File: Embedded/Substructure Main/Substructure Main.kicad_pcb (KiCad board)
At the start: 2 copper layers, 38 parts, among them U1 G0 FFC, U2 G1 FFC, U3 S FFC, U4 USB2513B_Bi, U5 MCP7940N-xMNY, U6 INA220AIDGSR

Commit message: Modified PCB Layout to allow component clusters
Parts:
- added C23: 22uF, Capacitor_SMD:C_0603_1608Metric_Pad1.08x0.95mm_HandSolder, F.Cu at (29.0, 169.9)
- added C24: 0.1uF, Capacitor_SMD:C_0603_1608Metric_Pad1.08x0.95mm_HandSolder, F.Cu at (29.0, 168.4)
- added C25: 1uF, Capacitor_SMD:C_0603_1608Metric_Pad1.08x0.95mm_HandSolder, F.Cu at (171.8, 173.0)
- added D1: WS2812B-2020, LED_SMD:LED_WS2812B-2020_PLCC4_2.0x2.0mm, F.Cu at (171.8, 175.0)
- added J1: MicroSD, Micro SD:MicroSD_473092651, F.Cu at (27.3, 172.4)
- added U8: F FFC, FFC:FFC-8-0.5, F.Cu at (114.0, 57.4)
- C1: footprint Capacitor_SMD:C_0603_1608Metric -> Capacitor_SMD:C_0603_1608Metric_Pad1.08x0.95mm_HandSolder
- moved C19 177.3 mm to (102.2, 171.6), turned to 180 degrees
- moved C17 173.9 mm to (96.1, 172.4), turned to 180 degrees
- moved U5 173.8 mm to (101.6, 173.6)
- moved C18 170.8 mm to (96.1, 173.9), turned to 180 degrees
- moved C21 160.8 mm to (63.2, 173.0), turned to 90 degrees
- moved R9 155.5 mm to (65.8, 173.8), turned to 180 degrees
- moved U6 152.8 mm to (57.2, 173.2)
- moved C20 152.4 mm to (58.8, 175.8), turned to 180 degrees
- moved R10 151.6 mm to (65.8, 172.2), turned to 180 degrees
- moved C16 37.0 mm to (140.0, 164.8), turned to -90 degrees
- moved C15 34.2 mm to (138.5, 164.8), turned to -90 degrees
- moved R7 31.5 mm to (139.3, 167.1), turned to 180 degrees
- moved C4 27.3 mm to (137.8, 179.2), turned to -90 degrees
- moved C7 25.4 mm to (136.5, 168.5), turned to 90 degrees
- moved C5 25.0 mm to (136.2, 179.2), turned to -90 degrees
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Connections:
- net USB2M renamed HUD USB -
- net USB2P renamed HUD USB +
- ESP1 pad 13: USB1P -> Main USB -
- ESP1 pad 14: USB1M -> Main USB +
- U1 pad 7: unconnected-(U1-Pad7) -> Photoresistor 1
- U2 pad 7: unconnected-(U2-Pad7) -> Photoresistor 2
- U4 pad 1: USB1M -> Main USB -
- U4 pad 2: USB1P -> Main USB +
- U4 pad 6: USB3M -> Snoot USB -
- U4 pad 7: USB3P -> Snoot USB +

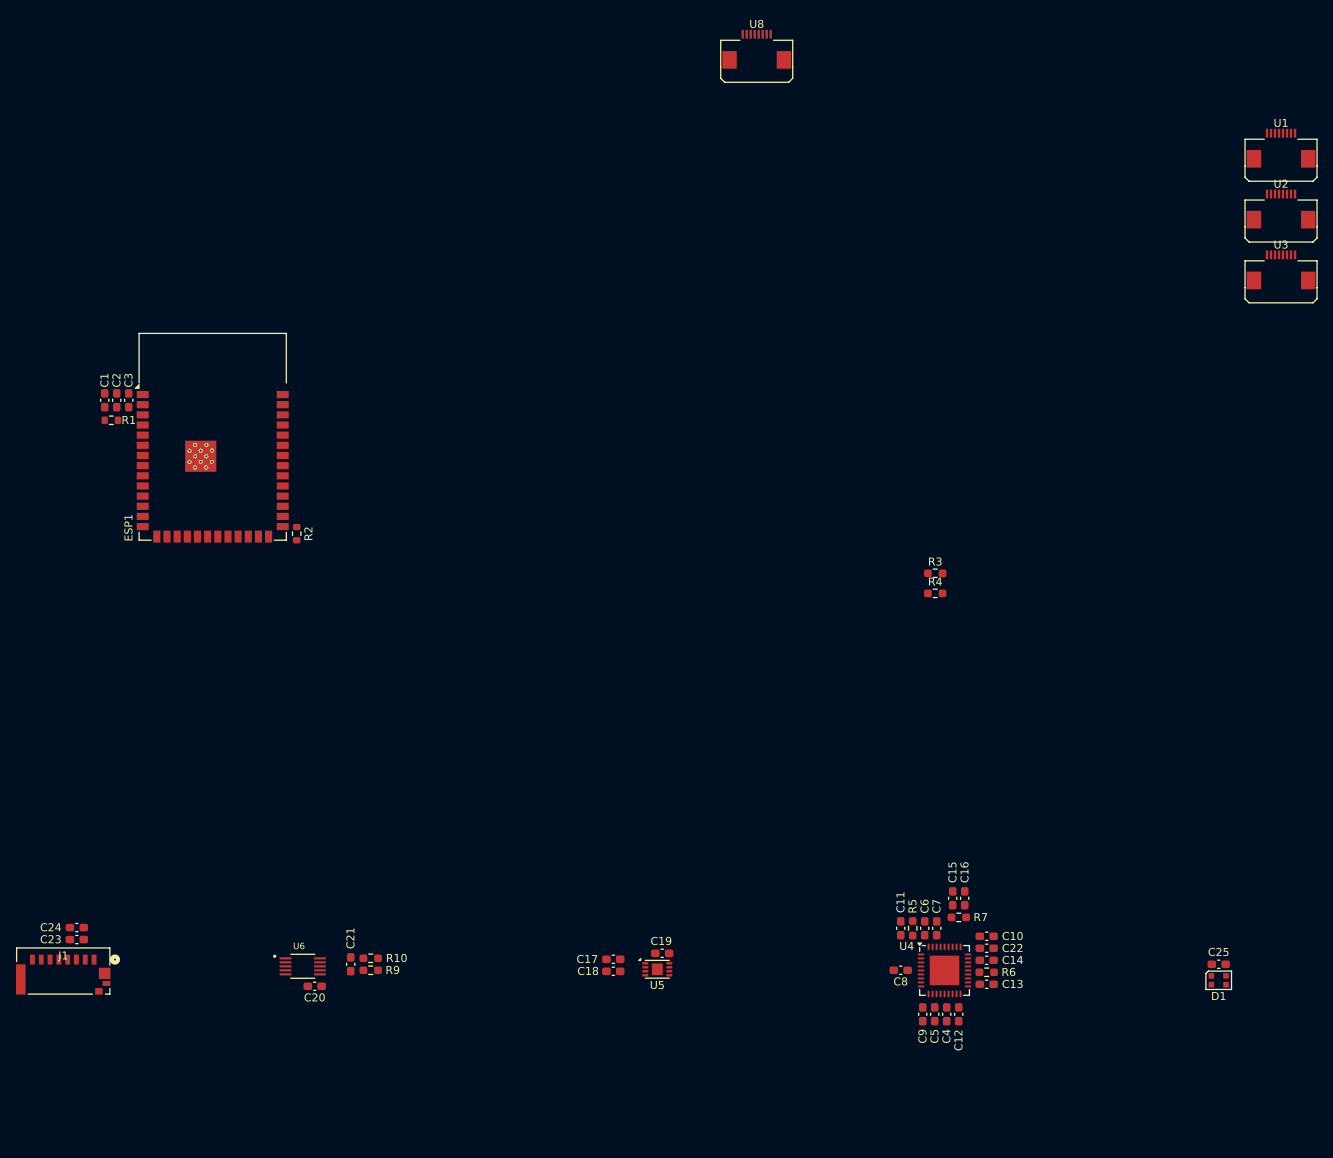
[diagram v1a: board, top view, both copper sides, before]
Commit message: Added Crystal Selection for RTC
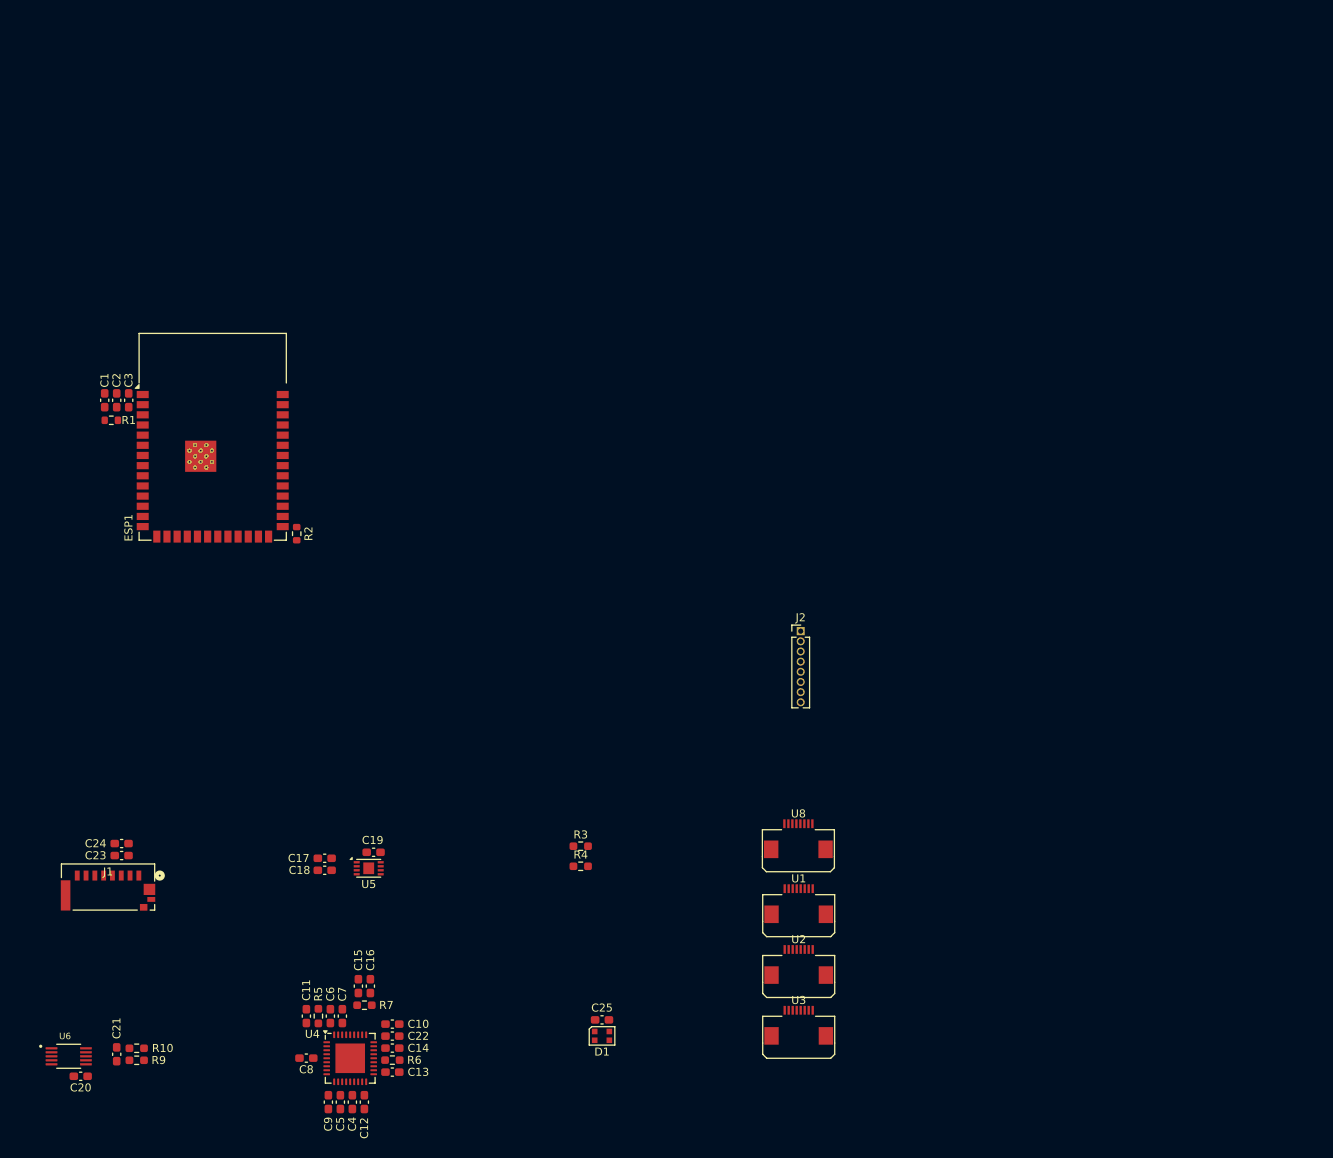
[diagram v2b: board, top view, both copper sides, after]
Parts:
- added J2: C Pins, Connector_PinHeader_1.27mm:PinHeader_1x08_P1.27mm_Vertical, F.Cu at (119.5, 131.4)
- moved U2 112.0 mm to (119.2, 171.8)
- moved U3 112.0 mm to (119.2, 179.4)
- moved U1 112.0 mm to (119.2, 164.2)
- moved U8 98.8 mm to (119.2, 156.1)
- moved C25 77.4 mm to (94.7, 179.9)
- moved D1 77.4 mm to (94.7, 181.9)
- moved C10 75.1 mm to (68.5, 180.5)
- moved C12 75.1 mm to (65.0, 190.2)
- moved C13 75.1 mm to (68.5, 186.5)
- moved C14 75.1 mm to (68.5, 183.5)
- moved C15 75.1 mm to (64.2, 175.7)
- moved C16 75.1 mm to (65.7, 175.7)
- moved C22 75.1 mm to (68.5, 182.0)
- moved R6 75.1 mm to (68.5, 185.0)
- moved R7 75.1 mm to (65.0, 178.1)
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
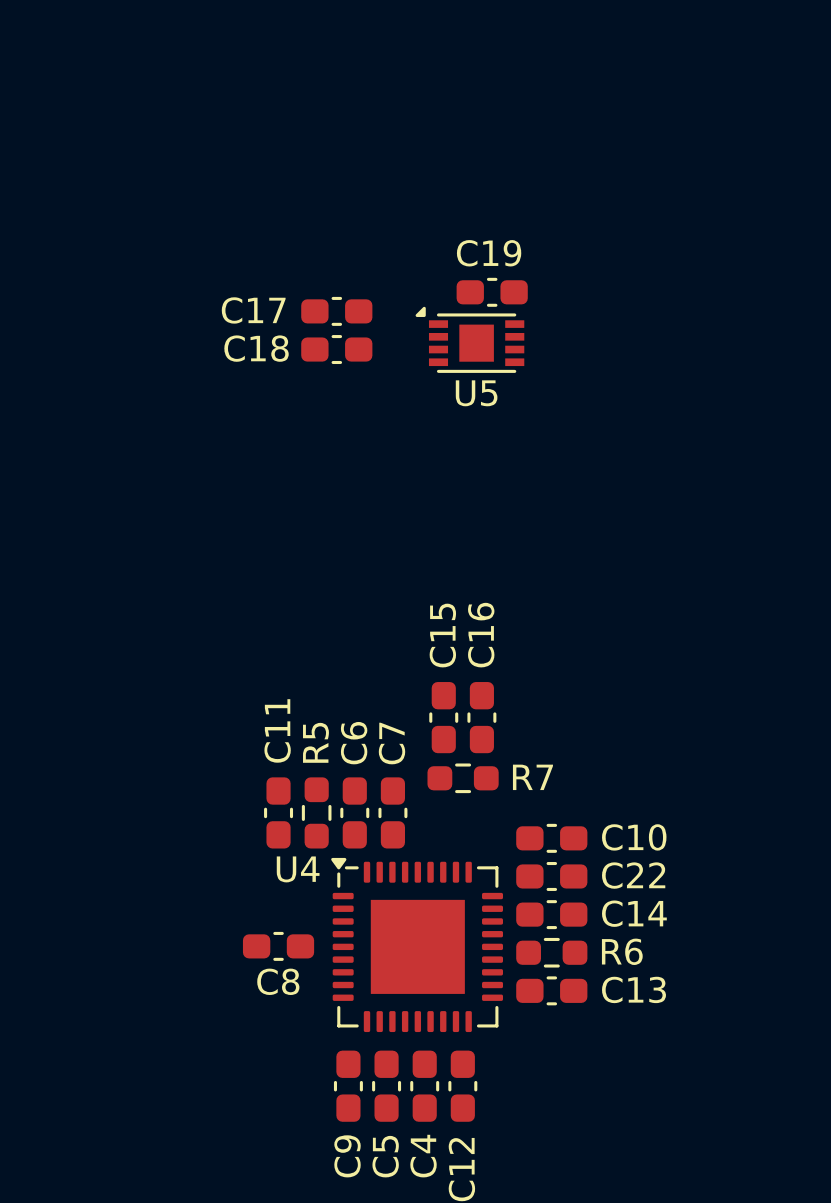
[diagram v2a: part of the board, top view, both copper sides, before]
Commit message: Added USB HUB Crystal
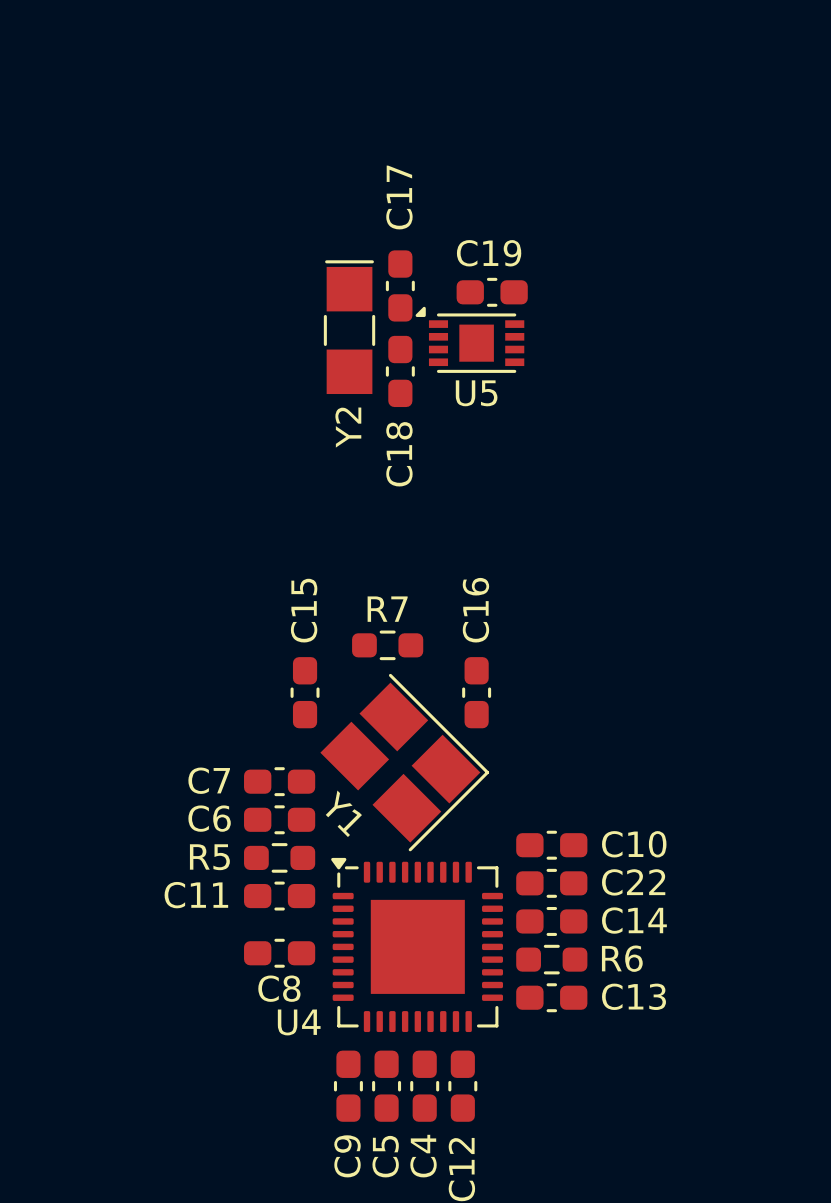
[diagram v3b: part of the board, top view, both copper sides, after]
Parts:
- added Y1: 24MHz 18pF, Crystal:Crystal_SMD_SeikoEpson_TSX3225-4Pin_3.2x2.5mm_HandSoldering, F.Cu at (62.5, 177.5)
- added Y2: 32.768KHz 8pf, Crystal:Crystal_SMD_MicroCrystal_CC7V-T1A-2Pin_3.2x1.5mm_HandSoldering, F.Cu at (60.5, 160.5)
- C17: value 18pf -> 10pf
- C18: value 18pf -> 12pf
- moved R7 6.01 mm to (62.0, 172.9)
- moved C15 5.54 mm to (58.8, 174.8)
- moved C7 4.62 mm to (57.8, 178.2), turned to 180 degrees
- moved C11 3.27 mm to (57.8, 182.8), turned to 180 degrees
- moved C6 2.97 mm to (57.8, 179.8), turned to 180 degrees
- moved C17 2.69 mm to (62.5, 158.8), turned to 90 degrees
- moved C18 2.64 mm to (62.5, 162.1), turned to -90 degrees
- moved R5 2.29 mm to (57.8, 181.2), turned to 0 degrees
- moved C16 1.00 mm to (65.5, 174.8)
- moved C8 0.27 mm to (57.8, 185.0)
- moved C10 0.27 mm to (68.5, 180.8)
- moved C13 0.27 mm to (68.5, 186.8)
- moved C14 0.27 mm to (68.5, 183.8)
- moved C22 0.27 mm to (68.5, 182.2)
- moved R6 0.27 mm to (68.5, 185.2)

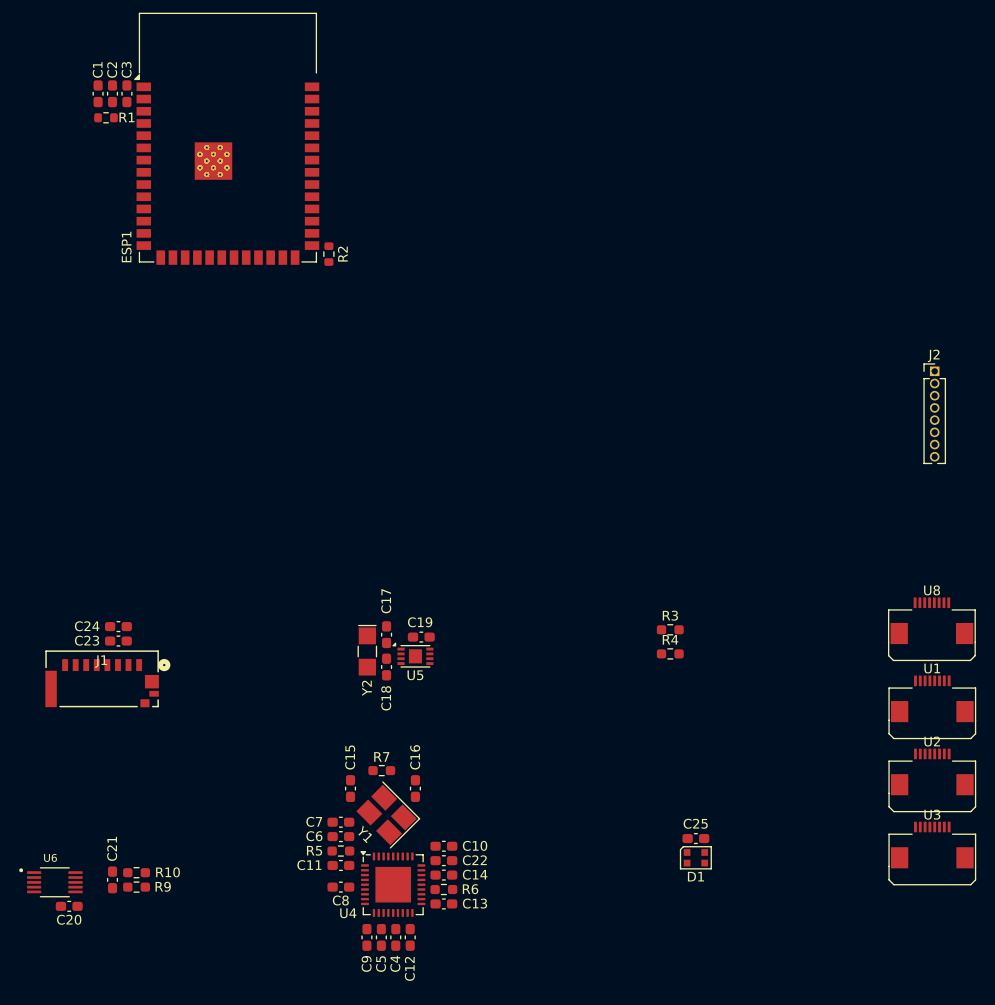
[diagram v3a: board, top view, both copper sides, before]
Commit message: Modified USB HUB Components from 0603 to 0402
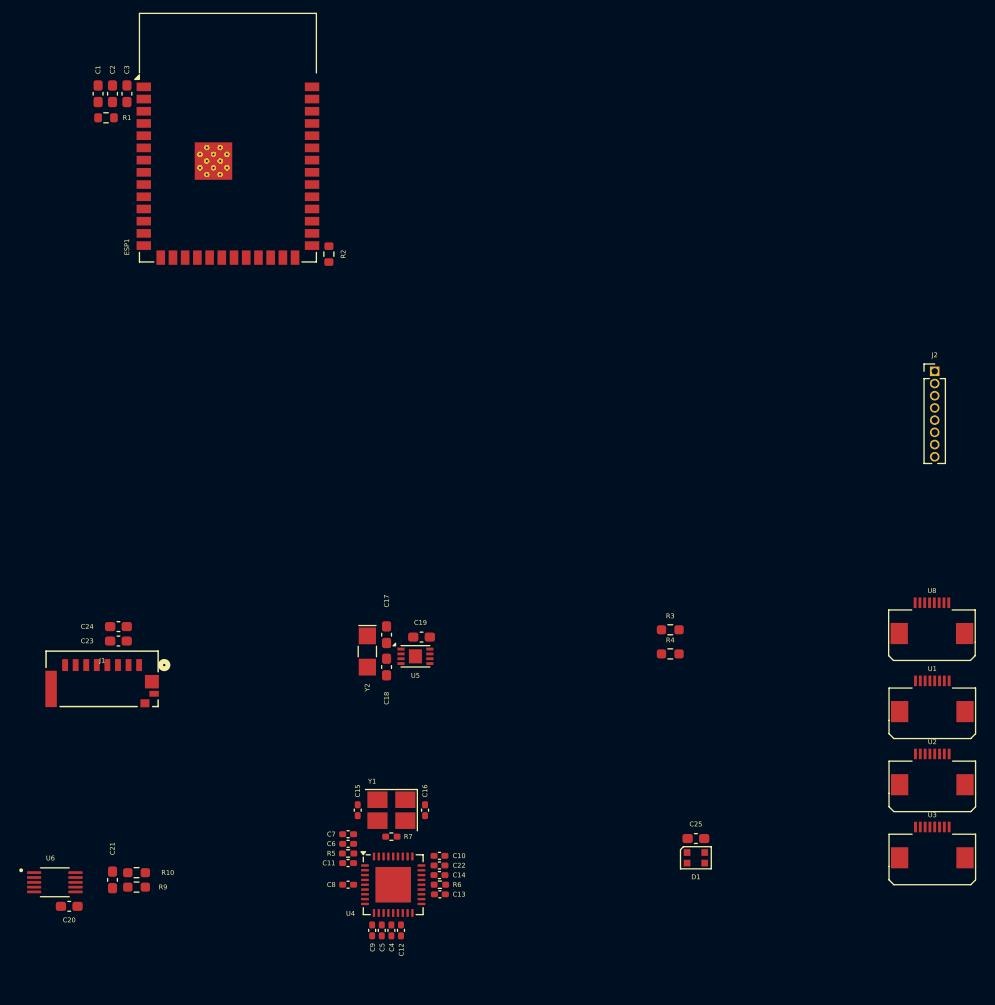
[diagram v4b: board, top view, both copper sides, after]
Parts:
- C10, C11, C12, C13, C14, C15, C16, C22, C4, C5, C6, C7, C8, C9: footprint Capacitor_SMD:C_0603_1608Metric_Pad1.08x0.95mm_HandSolder -> Capacitor_SMD:C_0402_1005Metric_Pad0.74x0.62mm_HandSolder
- R5, R6, R7: footprint Resistor_SMD:R_0603_1608Metric_Pad0.98x0.95mm_HandSolder -> Resistor_SMD:R_0402_1005Metric_Pad0.72x0.64mm_HandSolder
- moved R7 6.93 mm to (63.0, 179.8)
- moved C16 2.46 mm to (66.5, 177.0), turned to 90 degrees
- moved C15 2.37 mm to (59.5, 177.0)
- moved C7 1.46 mm to (58.5, 179.5)
- moved C12 1.20 mm to (64.0, 189.5)
- moved C10 1.10 mm to (68.0, 181.8)
- moved C13 1.08 mm to (68.0, 185.8), turned to 180 degrees
- moved C6 1.06 mm to (58.5, 180.5)
- moved C9 0.91 mm to (61.0, 189.5)
- moved C4 0.86 mm to (63.0, 189.5)
- moved C11 0.79 mm to (58.5, 182.5)
- moved C8 0.79 mm to (58.5, 184.8)
- moved R5 0.79 mm to (58.5, 181.5)
- moved C5 0.73 mm to (62.0, 189.5)
- moved Y1 0.71 mm to (63.0, 177.0), turned to 180 degrees
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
